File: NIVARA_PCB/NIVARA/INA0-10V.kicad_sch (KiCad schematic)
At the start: 0 parts

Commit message: avance
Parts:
- added C6: 100nF, PCM_Capacitor_SMD_AKL:C_0603_1608Metric, symbol PCM_Capacitor_AKL:C_0603
- added R3: 22K, PCM_Resistor_SMD_AKL:R_0603_1608Metric, symbol PCM_Resistor_AKL:R_0603
- added R41: 10K, PCM_Resistor_SMD_AKL:R_0603_1608Metric, symbol PCM_Resistor_AKL:R_0603
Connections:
- net IN_1: now also R3.1
- net OUT_1: now also C6.2, R3.2, R41.1
- new net GND: C6.1, R41.2
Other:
- note added: "0-10V"

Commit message: ACTUALIZACION
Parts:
- C6: PART NUMBERT (none) -> CC0603KRX7R9BB104
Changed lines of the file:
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@@
 			)
 		)
-		(property "PART NUMBERT" ""
+		(property "PART NUMBERT" "CC0603KRX7R9BB104"
 			(at 44.45 41.91 0)
 			(effects

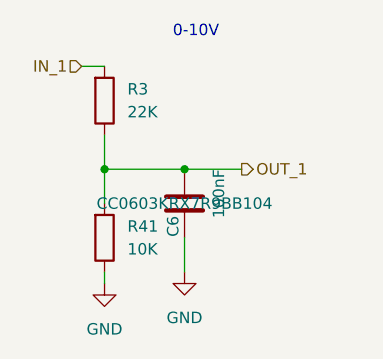
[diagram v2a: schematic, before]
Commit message: Se organizaron componentes en el area de PCB
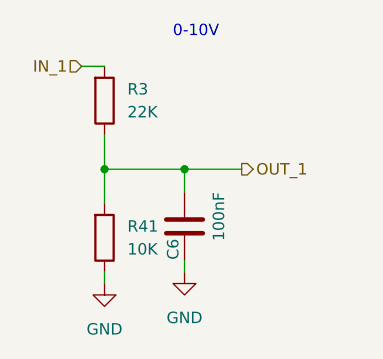
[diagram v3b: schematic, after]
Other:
- moved on the sheet: C6
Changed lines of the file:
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@@
 	(wire
 		(pts
-			(xy 44.45 49.53) (xy 44.45 45.72)
+			(xy 44.45 40.64) (xy 44.45 38.1)
+		)
+		(stroke
+			(width 0)
+			(type default)
+		)
+	)
+	(wire
+		(pts
+			(xy 44.45 49.53) (xy 44.45 48.26)
 		)
 		(stroke
@@
 	(symbol
 		(lib_id "PCM_Capacitor_AKL:C_0603")
-		(at 44.45 41.91 180)
+		(at 44.45 44.45 180)
 		(unit 1)
 		(exclude_from_sim no)
@@
 		(dnp no)
 		(property "Reference" "C6"
-			(at 43.18 44.45 90)
+			(at 43.18 46.99 90)
 			(effects
 				(font
@@
 		)
 		(property "Value" "100nF"
-			(at 48.26 38.1 90)
+			(at 48.26 40.64 90)
 			(effects
 				(font
@@
 		)
 		(property "Footprint" "PCM_Capacitor_SMD_AKL:C_0603_1608Metric"
-			(at 43.4848 38.1 0)
+			(at 43.4848 40.64 0)
 			(effects
 				(font
@@
 		)
 		(property "Datasheet" "~"
-			(at 44.45 41.91 0)
+			(at 44.45 44.45 0)
 			(effects
 				(font
@@
 		)
 		(property "Description" "SMD 0603 MLCC capacitor, Alternate KiCad Library"
-			(at 44.45 41.91 0)
+			(at 44.45 44.45 0)
 			(effects
 				(font
@@
 		)
 		(property "PART NUMBERT" "CC0603KRX7R9BB104"
-			(at 44.45 41.91 0)
-			(effects
-				(font
-					(size 1.27 1.27)
-				)
-			)
-		)
+			(at 44.45 44.45 0)
+			(effects
+				(font
+					(size 1.27 1.27)
+				)
+				(hide yes)
+			)
+		)
